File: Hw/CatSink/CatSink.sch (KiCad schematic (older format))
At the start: 36 parts, among them J1 Vout, P1 USB_C_Plug_USB2.0, Q1 SI3421DV, Q2 SI3421DV, SW1 Voltage, SW2 Curent, U1 CYPD3177-24LQXI

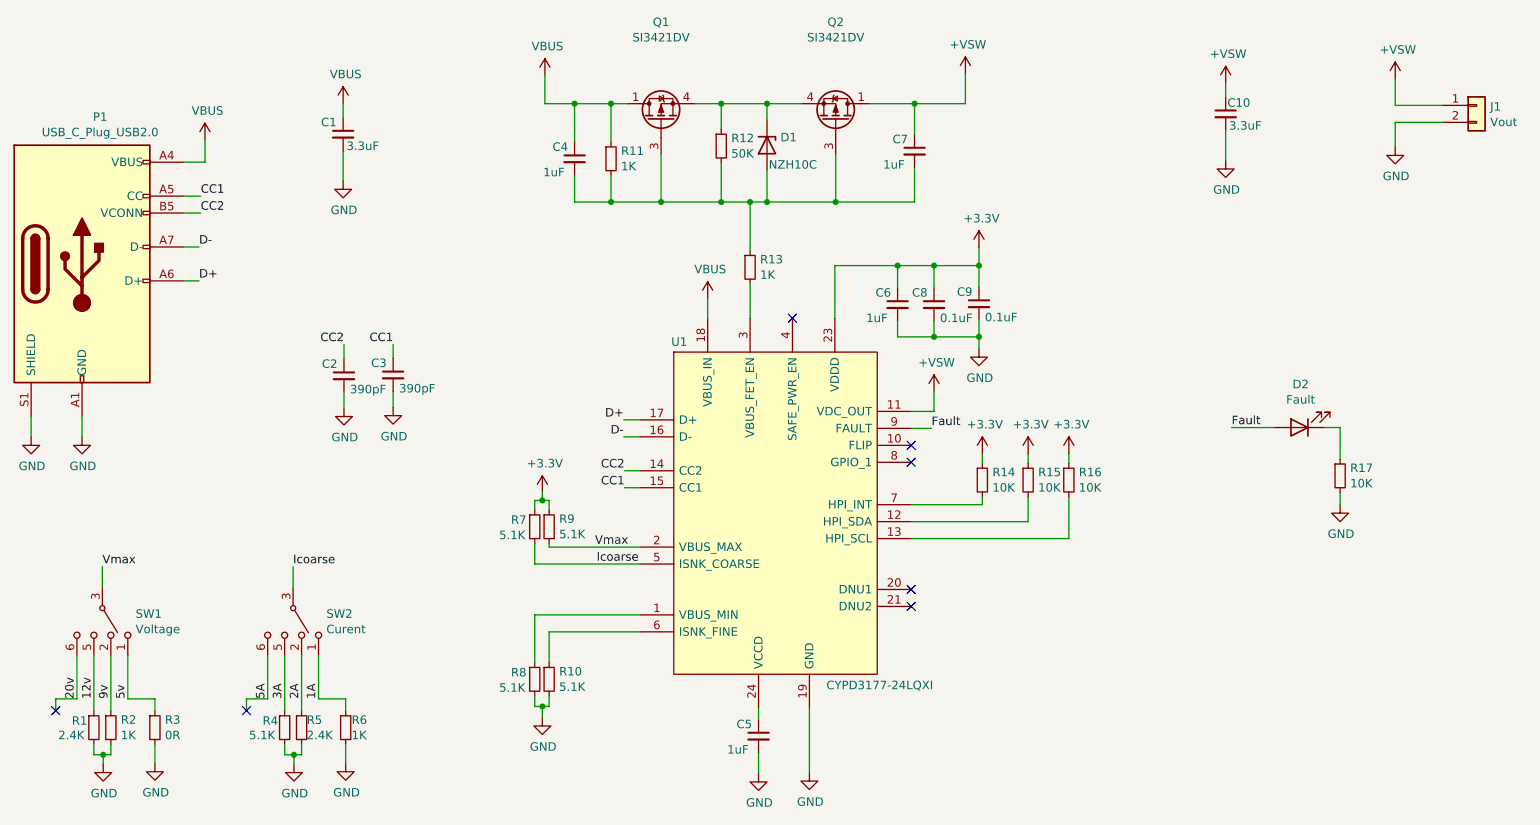
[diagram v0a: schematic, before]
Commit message: Added Led and 3D switch
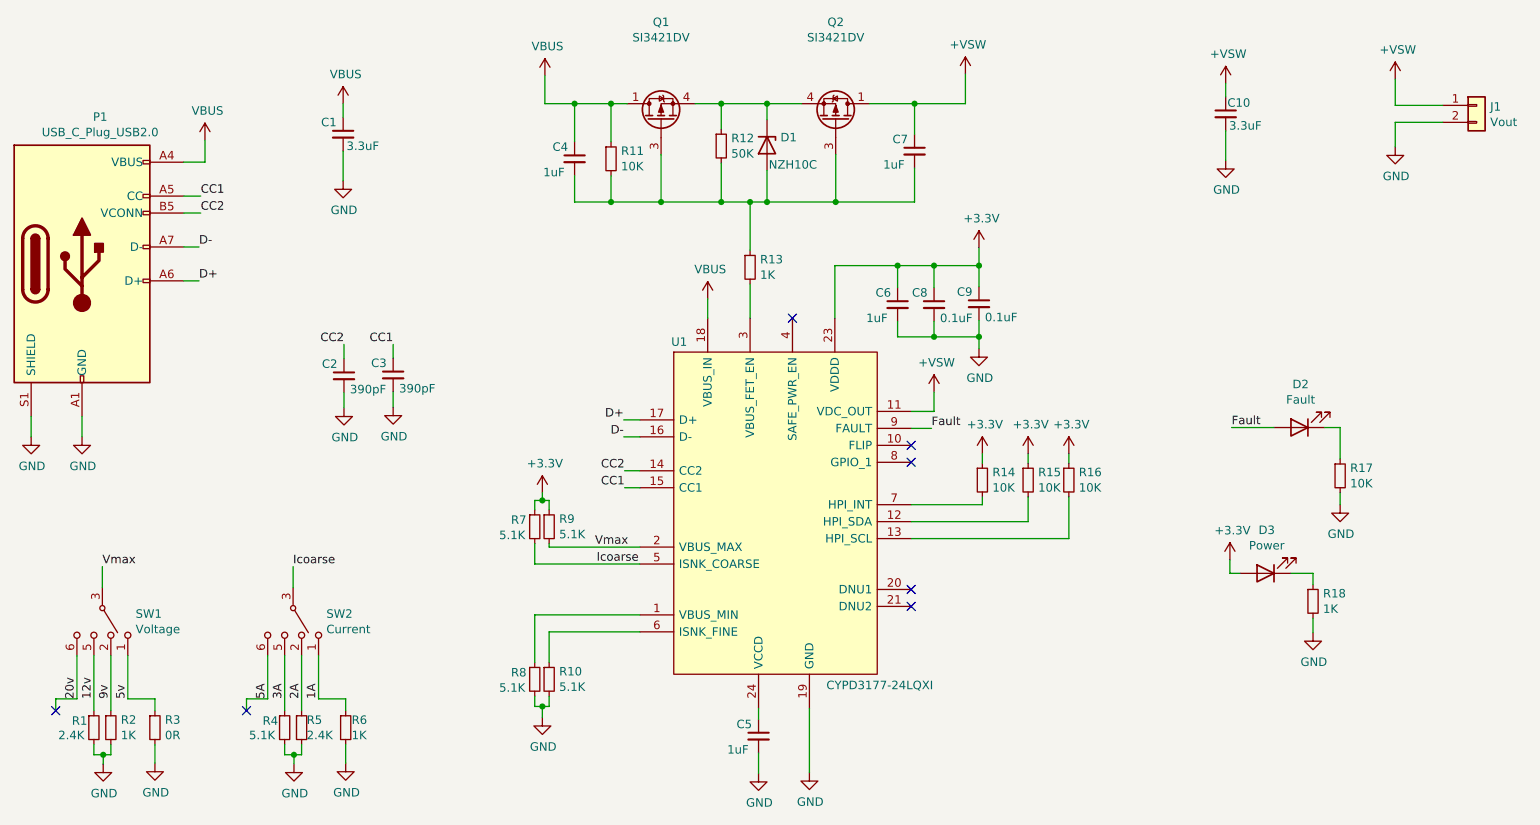
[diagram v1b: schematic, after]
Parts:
- added D3: Power, LED_SMD:LED_0603_1608Metric, symbol Device:LED
- added R18: 1K, Resistor_SMD:R_0603_1608Metric, symbol Device:R_Small
- R11: value 1K -> 10K
- SW2: value Curent -> Current
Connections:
- net +3V3: now also D3.2 (A)
- net GND: now also R18.2
- new net: D3.1 (K), R18.1
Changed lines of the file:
@@
 P 4485 1460
 F 0 "R11" H 4544 1506 50  0000 L CNN
-F 1 "1K" H 4544 1415 50  0000 L CNN
+F 1 "10K" H 4544 1415 50  0000 L CNN
 F 2 "Resistor_SMD:R_0603_1608Metric" H 4485 1460 50  0001 C CNN
 F 3 "~" H 4485 1460 50  0001 C CNN
@@
 P 2610 4190
 F 0 "SW2" V 2564 4386 50  0000 L CNN
-F 1 "Curent" V 2655 4386 50  0000 L CNN
+F 1 "Current" V 2655 4386 50  0000 L CNN
 F 2 "CatSink:K3-1410S-E1" H 1985 4365 50  0001 C CNN
 F 3 "~" H 1985 4365 50  0001 C CNN
@@
 	1    0    0    -1
 $EndComp
+$Comp
+L Device:R_Small R18
+U 1 1 5F9A5CE1
+P 8625 4070
+F 0 "R18" H 8684 4116 50  0000 L CNN
+F 1 "1K" H 8684 4025 50  0000 L CNN
+F 2 "Resistor_SMD:R_0603_1608Metric" H 8625 4070 50  0001 C CNN
+F 3 "~" H 8625 4070 50  0001 C CNN
+	1    8625 4070
+	1    0    0    -1
+$EndComp
+$Comp
+L Device:LED D3
+U 1 1 5F9A5F37
+P 8345 3905
+F 0 "D3" H 8338 3650 50  0000 C CNN
+F 1 "Power" H 8338 3741 50  0000 C CNN
+F 2 "LED_SMD:LED_0603_1608Metric" H 8345 3905 50  0001 C CNN
+F 3 "~" H 8345 3905 50  0001 C CNN
+	1    8345 3905
+	-1   0    0    1
+$EndComp
+Wire Wire Line
+	8495 3905 8625 3905
+Wire Wire Line
+	8625 3905 8625 3970
+$Comp
+L power:GND #PWR0101
+U 1 1 5F9B2DA0
+P 8625 4255
+F 0 "#PWR0101" H 8625 4005 50  0001 C CNN
+F 1 "GND" H 8630 4082 50  0000 C CNN
+F 2 "" H 8625 4255 50  0001 C CNN
+F 3 "" H 8625 4255 50  0001 C CNN
+	1    8625 4255
+	1    0    0    -1
+$EndComp
+Wire Wire Line
+	8625 4170 8625 4255
+$Comp
+L power:+3.3V #PWR0102
+U 1 1 5F9C11CD
+P 8135 3825
+F 0 "#PWR0102" H 8135 3675 50  0001 C CNN
+F 1 "+3.3V" H 8150 3998 50  0000 C CNN
+F 2 "" H 8135 3825 50  0001 C CNN
+F 3 "" H 8135 3825 50  0001 C CNN
+	1    8135 3825
+	1    0    0    -1
+$EndComp
+Wire Wire Line
+	8195 3905 8135 3905
+Wire Wire Line
+	8135 3905 8135 3825
 $EndSCHEMATC

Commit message: update BOM
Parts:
- C1, C10: lcsc (none) -> C76663
- C2, C3: lcsc (none) -> C376830
- C4, C5, C6, C7: lcsc (none) -> C26413
- C8, C9: lcsc (none) -> C235731
- D1: lcsc C551630 -> (none)
- D2: lcsc (none) -> C138541
- D3: lcsc (none) -> C118330
- P1: lcsc (none) -> C393939
- R1, R5: lcsc (none) -> C98728
- R10, R4, R7, R8, R9: lcsc (none) -> C131715
- R11, R14, R15, R16, R17: lcsc (none) -> C217281
- R12: lcsc (none) -> C304067
- R13, R18, R2, R6: lcsc (none) -> C517454
- R3: manf# (none) -> ERJ-3GEY0R00V
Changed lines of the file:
@@
 F 2 "Connectors:C393939" H 1515 2080 50  0001 C CNN
 F 3 "https://www.usb.org/sites/default/files/documents/usb_type-c.zip" H 1515 2080 50  0001 C CNN
+F 4 "C393939" H 1365 2080 50  0001 C CNN "lcsc"
 	1    1365 2080
 	1    0    0    -1
@@
 F 2 "Capacitor_SMD:C_0603_1608Metric" H 5355 4865 50  0001 C CNN
 F 3 "~" H 5355 4865 50  0001 C CNN
+F 4 "C26413" H 5355 4865 50  0001 C CNN "lcsc"
 	1    5355 4865
 	1    0    0    -1
@@
 F 2 "Capacitor_SMD:C_0603_1608Metric" H 6175 2320 50  0001 C CNN
 F 3 "~" H 6175 2320 50  0001 C CNN
+F 4 "C26413" H 6175 2320 50  0001 C CNN "lcsc"
 	1    6175 2320
 	1    0    0    -1
@@
 F 2 "Capacitor_SMD:C_0603_1608Metric" H 6390 2320 50  0001 C CNN
 F 3 "~" H 6390 2320 50  0001 C CNN
+F 4 "C235731" H 6390 2320 50  0001 C CNN "lcsc"
 	1    6390 2320
 	1    0    0    -1
@@
 F 2 "Capacitor_SMD:C_0603_1608Metric" H 6655 2315 50  0001 C CNN
 F 3 "~" H 6655 2315 50  0001 C CNN
+F 4 "C235731" H 6655 2315 50  0001 C CNN "lcsc"
 	1    6655 2315
 	1    0    0    -1
@@
 F 2 "Resistor_SMD:R_0603_1608Metric" H 5305 2100 50  0001 C CNN
 F 3 "~" H 5305 2100 50  0001 C CNN
+F 4 "C517454" H 5305 2100 50  0001 C CNN "lcsc"
 	1    5305 2100
 	1    0    0    -1
@@
 F 2 "Capacitor_SMD:C_0603_1608Metric" H 3200 2735 50  0001 C CNN
 F 3 "~" H 3200 2735 50  0001 C CNN
+F 4 "C376830" H 3200 2735 50  0001 C CNN "lcsc"
 	1    3200 2735
 	1    0    0    -1
@@
 F 2 "Capacitor_SMD:C_0603_1608Metric" H 2910 2740 50  0001 C CNN
 F 3 "~" H 2910 2740 50  0001 C CNN
+F 4 "C376830" H 2910 2740 50  0001 C CNN "lcsc"
 	1    2910 2740
 	1    0    0    -1
@@
 F 3 "~" H 5405 1380 50  0001 C CNN
 F 4 "NZH10C,115" H 5405 1380 50  0001 C CNN "manf#"
-F 5 "C551630" H 5405 1380 50  0001 C CNN "lcsc"
+F 5 "" H 5405 1380 50  0001 C CNN "lcsc"
 	1    5405 1380
 	0    1    1    0
@@
 F 2 "Resistor_SMD:R_0603_1608Metric" H 5135 1385 50  0001 C CNN
 F 3 "~" H 5135 1385 50  0001 C CNN
+F 4 "C304067" H 5135 1385 50  0001 C CNN "lcsc"
 	1    5135 1385
 	1    0    0    -1
@@
 F 2 "Resistor_SMD:R_0603_1608Metric" H 4485 1460 50  0001 C CNN
 F 3 "~" H 4485 1460 50  0001 C CNN
+F 4 "C217281" H 4485 1460 50  0001 C CNN "lcsc"
 	1    4485 1460
 	1    0    0    -1
@@
 F 2 "Capacitor_SMD:C_0603_1608Metric" H 4270 1460 50  0001 C CNN
 F 3 "~" H 4270 1460 50  0001 C CNN
+F 4 "C26413" H 4270 1460 50  0001 C CNN "lcsc"
 	1    4270 1460
 	1    0    0    -1
@@
 F 2 "Capacitor_SMD:C_0603_1608Metric" H 6275 1415 50  0001 C CNN
 F 3 "~" H 6275 1415 50  0001 C CNN
+F 4 "C26413" H 6275 1415 50  0001 C CNN "lcsc"
 	1    6275 1415
 	1    0    0    -1
@@
 F 2 "Resistor_SMD:R_0603_1608Metric" H 4120 3630 50  0001 C CNN
 F 3 "~" H 4120 3630 50  0001 C CNN
+F 4 "C131715" H 4120 3630 50  0001 C CNN "lcsc"
 	1    4120 3630
 	1    0    0    -1
@@
 F 2 "Resistor_SMD:R_0603_1608Metric" H 4035 3630 50  0001 C CNN
 F 3 "~" H 4035 3630 50  0001 C CNN
+F 4 "C131715" H 4035 3630 50  0001 C CNN "lcsc"
 	1    4035 3630
 	1    0    0    -1
@@
 F 2 "Resistor_SMD:R_0603_1608Metric" H 4120 4530 50  0001 C CNN
 F 3 "~" H 4120 4530 50  0001 C CNN
+F 4 "C131715" H 4120 4530 50  0001 C CNN "lcsc"
 	1    4120 4530
 	1    0    0    -1
@@
 F 2 "Resistor_SMD:R_0603_1608Metric" H 4035 4530 50  0001 C CNN
 F 3 "~" H 4035 4530 50  0001 C CNN
+F 4 "C131715" H 4035 4530 50  0001 C CNN "lcsc"
 	1    4035 4530
 	1    0    0    -1
@@
 F 2 "Capacitor_SMD:C_1206_3216Metric" H 2905 1315 50  0001 C CNN
 F 3 "~" H 2905 1315 50  0001 C CNN
+F 4 "C76663" H 2905 1315 50  0001 C CNN "lcsc"
 	1    2905 1315
 	1    0    0    -1
@@
 F 2 "Resistor_SMD:R_0603_1608Metric" H 6945 3355 50  0001 C CNN
 F 3 "~" H 6945 3355 50  0001 C CNN
+F 4 "C217281" H 6945 3355 50  0001 C CNN "lcsc"
 	1    6945 3355
 	1    0    0    -1
@@
 F 2 "Resistor_SMD:R_0603_1608Metric" H 7185 3355 50  0001 C CNN
 F 3 "~" H 7185 3355 50  0001 C CNN
+F 4 "C217281" H 7185 3355 50  0001 C CNN "lcsc"
 	1    7185 3355
 	1    0    0    -1
@@
 F 2 "LED_SMD:LED_0603_1608Metric" H 8545 3045 50  0001 C CNN
 F 3 "~" H 8545 3045 50  0001 C CNN
+F 4 "C138541" H 8545 3045 50  0001 C CNN "lcsc"
 	1    8545 3045
 	-1   0    0    1
@@
 F 2 "Resistor_SMD:R_0603_1608Metric" H 8785 3330 50  0001 C CNN
 F 3 "~" H 8785 3330 50  0001 C CNN
+F 4 "C217281" H 8785 3330 50  0001 C CNN "lcsc"
 	1    8785 3330
 	1    0    0    -1
@@
 F 2 "Resistor_SMD:R_0603_1608Metric" H 1795 4815 50  0001 C CNN
 F 3 "~" H 1795 4815 50  0001 C CNN
+F 4 "ERJ-3GEY0R00V" H 1795 4815 50  0001 C CNN "manf#"
 	1    1795 4815
 	1    0    0    -1
@@
 F 2 "Resistor_SMD:R_0603_1608Metric" H 1535 4815 50  0001 C CNN
 F 3 "~" H 1535 4815 50  0001 C CNN
+F 4 "C517454" H 1535 4815 50  0001 C CNN "lcsc"
 	1    1535 4815
 	1    0    0    -1
@@
 F 2 "Resistor_SMD:R_0603_1608Metric" H 1435 4815 50  0001 C CNN
 F 3 "~" H 1435 4815 50  0001 C CNN
+F 4 "C98728" H 1435 4815 50  0001 C CNN "lcsc"
 	1    1435 4815
 	1    0    0    -1
@@
 F 2 "Resistor_SMD:R_0603_1608Metric" H 2920 4815 50  0001 C CNN
 F 3 "~" H 2920 4815 50  0001 C CNN
+F 4 "C517454" H 2920 4815 50  0001 C CNN "lcsc"
 	1    2920 4815
 	1    0    0    -1
@@
 F 2 "Resistor_SMD:R_0603_1608Metric" H 2660 4815 50  0001 C CNN
 F 3 "~" H 2660 4815 50  0001 C CNN
+F 4 "C98728" H 2660 4815 50  0001 C CNN "lcsc"
 	1    2660 4815
 	1    0    0    -1
@@
 F 2 "Resistor_SMD:R_0603_1608Metric" H 2560 4815 50  0001 C CNN
 F 3 "~" H 2560 4815 50  0001 C CNN
+F 4 "C131715" H 2560 4815 50  0001 C CNN "lcsc"
 	1    2560 4815
 	1    0    0    -1
@@
 F 2 "Capacitor_SMD:C_1206_3216Metric" H 8110 1195 50  0001 C CNN
 F 3 "~" H 8110 1195 50  0001 C CNN
+F 4 "C76663" H 8110 1195 50  0001 C CNN "lcsc"
 	1    8110 1195
 	1    0    0    -1
@@
 F 2 "Resistor_SMD:R_0603_1608Metric" H 6675 3355 50  0001 C CNN
 F 3 "~" H 6675 3355 50  0001 C CNN
+F 4 "C217281" H 6675 3355 50  0001 C CNN "lcsc"
 	1    6675 3355
 	1    0    0    -1
@@
 F 2 "Resistor_SMD:R_0603_1608Metric" H 8625 4070 50  0001 C CNN
 F 3 "~" H 8625 4070 50  0001 C CNN
+F 4 "C517454" H 8625 4070 50  0001 C CNN "lcsc"
 	1    8625 4070
 	1    0    0    -1
@@
 F 2 "LED_SMD:LED_0603_1608Metric" H 8345 3905 50  0001 C CNN
 F 3 "~" H 8345 3905 50  0001 C CNN
+F 4 "C118330" H 8345 3905 50  0001 C CNN "lcsc"
 	1    8345 3905
 	-1   0    0    1

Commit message: update kicad project
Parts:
- P1: symbol Connector:USB_C_Plug_USB2.0 -> CatSink-rescue:USB_C_Plug_USB2.0-Connector
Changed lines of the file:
@@
 $EndComp
 $Comp
-L Connector:USB_C_Plug_USB2.0 P1
+L CatSink-rescue:USB_C_Plug_USB2.0-Connector P1
 U 1 1 5F957B03
 P 1365 2080
